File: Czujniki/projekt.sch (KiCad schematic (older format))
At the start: 79 parts, among them P1 CONN_01X08, P2 CONN_01X06, P3 CONN_01X05, T1 Si2323DS, T2 FDV303N, T3 FDV303N, T4 Si2323DS, T5 Si2323DS, T6 Si2323DS, T7 Si2323DS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

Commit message: All things on PCB.
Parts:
- removed DET2: MQ-Sensor, symbol MQ-Sensor
- removed R11: R, symbol R
- removed R12: 100K, symbol R_Small
- removed T6, T7: Si2323DS, symbol Si2323DS
- C10, C9: footprint (none) -> Capacitors_SMD:C_0805_HandSoldering
- DET1: footprint (none) -> Footprinty:MQ-sensor
- R10, R9: footprint (none) -> Resistors_SMD:R_0603
- T4, T5: footprint (none) -> Footprinty:SOT23
- U5: footprint (none) -> Footprinty:SOT23-mcp1700
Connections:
- no-connect marks 6 -> 8
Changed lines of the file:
@@
 $EndComp
-$Comp
-L MQ-Sensor DET2
-U 1 1 55B21DD7
-P 4900 8650
-F 0 "DET2" H 5050 8800 60  0000 C CNN
-F 1 "MQ-Sensor" V 4750 8350 60  0000 C CNN
-F 2 "" H 4900 8650 60  0000 C CNN
-F 3 "" H 4900 8650 60  0000 C CNN
-	1    4900 8650
-	1    0    0    -1
-$EndComp
-$Comp
-L R R11
-U 1 1 55B22225
-P 5150 8850
-F 0 "R11" V 5230 8850 50  0000 C CNN
-F 1 "R" V 5150 8850 50  0000 C CNN
-F 2 "" V 5080 8850 30  0000 C CNN
-F 3 "" H 5150 8850 30  0000 C CNN
-	1    5150 8850
-	1    0    0    -1
-$EndComp
-Wire Wire Line
-	5100 8650 5200 8650
-Wire Wire Line
-	5150 8650 5150 8700
 $Comp
 L MCP1702 U5
@@
 F 0 "U5" H 1950 5950 60  0000 C CNN
 F 1 "MCP1702" H 1850 6200 60  0000 C CNN
-F 2 "" H 1850 6050 60  0000 C CNN
+F 2 "Footprinty:SOT23-mcp1700" H 1850 6050 60  0001 C CNN
 F 3 "" H 1850 6050 60  0000 C CNN
 	1    1850 6100
 	1    0    0    -1
 $EndComp
-$Comp
-L Si2323DS T7
-U 1 1 55B2543A
-P 4900 8200
-F 0 "T7" H 4750 8350 39  0000 C CNN
-F 1 "Si2323DS" V 4950 8200 39  0000 C CNN
-F 2 "" H 4900 8200 39  0000 C CNN
-F 3 "" H 4900 8200 39  0000 C CNN
-	1    4900 8200
-	-1   0    0    1
-$EndComp
-Wire Wire Line
-	4900 7900 4900 8000
-$Comp
-L R_Small R12
-U 1 1 55B260F1
-P 5300 8200
-F 0 "R12" H 5330 8220 50  0000 L CNN
-F 1 "100K" H 5330 8160 50  0000 L CNN
-F 2 "" H 5300 8200 60  0000 C CNN
-F 3 "" H 5300 8200 60  0000 C CNN
-	1    5300 8200
-	0    -1   -1   0
-$EndComp
-Wire Wire Line
-	5100 8200 5200 8200
-Text GLabel 5450 8200 2    39   Input ~ 0
-DRV2
-Wire Wire Line
-	5450 8200 5400 8200
 $Comp
 L VDD #PWR076
@@
 $EndComp
 $Comp
-L GND #PWR078
-U 1 1 55B282A9
-P 5150 9050
-F 0 "#PWR078" H 5150 8800 50  0001 C CNN
-F 1 "GND" H 5150 8900 50  0000 C CNN
-F 2 "" H 5150 9050 60  0000 C CNN
-F 3 "" H 5150 9050 60  0000 C CNN
-	1    5150 9050
-	1    0    0    -1
-$EndComp
-Wire Wire Line
-	5150 9000 5150 9050
-$Comp
-L GND #PWR079
-U 1 1 55B28E36
-P 4900 9050
-F 0 "#PWR079" H 4900 8800 50  0001 C CNN
-F 1 "GND" H 4900 8900 50  0000 C CNN
-F 2 "" H 4900 9050 60  0000 C CNN
-F 3 "" H 4900 9050 60  0000 C CNN
-	1    4900 9050
-	1    0    0    -1
-$EndComp
-Wire Wire Line
-	4900 9050 4900 8850
-$Comp
-L Si2323DS T6
-U 1 1 55B29516
-P 4500 8200
-F 0 "T6" H 4350 8350 39  0000 C CNN
-F 1 "Si2323DS" V 4550 8200 39  0000 C CNN
-F 2 "" H 4500 8200 39  0000 C CNN
-F 3 "" H 4500 8200 39  0000 C CNN
-	1    4500 8200
-	-1   0    0    1
-$EndComp
-Wire Wire Line
-	4900 8400 4900 8450
-Wire Wire Line
-	5150 7950 5150 8200
-Wire Wire Line
-	5150 7950 4750 7950
-Wire Wire Line
-	4750 7950 4750 8200
-Wire Wire Line
-	4750 8200 4700 8200
-Connection ~ 5150 8200
-$Comp
 L VPP #PWR080
 U 1 1 55B2B4BE
@@
 $EndComp
 Wire Wire Line
-	4500 8000 4500 7900
-$Comp
-L VPP #PWR081
-U 1 1 55B2CA0B
-P 4900 7900
-F 0 "#PWR081" H 4900 7750 50  0001 C CNN
-F 1 "VPP" H 4900 8050 50  0000 C CNN
-F 2 "" H 4900 7900 60  0000 C CNN
-F 3 "" H 4900 7900 60  0000 C CNN
-	1    4900 7900
-	1    0    0    -1
-$EndComp
-Wire Wire Line
-	4500 8400 4500 8650
-Wire Wire Line
-	4500 8650 4700 8650
-$Comp
-L +5V #PWR082
-U 1 1 55B2D445
-P 4500 7900
-F 0 "#PWR082" H 4500 7750 50  0001 C CNN
-F 1 "+5V" H 4500 8040 50  0000 C CNN
-F 2 "" H 4500 7900 60  0000 C CNN
-F 3 "" H 4500 7900 60  0000 C CNN
-	1    4500 7900
-	1    0    0    -1
-$EndComp
-Wire Wire Line
 	2250 6050 2250 6150
 Wire Wire Line
@@
 F 0 "C10" H 2260 6320 50  0000 L CNN
 F 1 "1U" H 2260 6170 50  0000 L CNN
-F 2 "" H 2250 6250 60  0000 C CNN
+F 2 "Capacitors_SMD:C_0805_HandSoldering" H 2250 6250 60  0001 C CNN
 F 3 "" H 2250 6250 60  0000 C CNN
 	1    2250 6250
@@
 F 0 "C9" H 1460 6320 50  0000 L CNN
 F 1 "1U" H 1460 6170 50  0000 L CNN
-F 2 "" H 1450 6250 60  0000 C CNN
+F 2 "Capacitors_SMD:C_0805_HandSoldering" H 1450 6250 60  0001 C CNN
 F 3 "" H 1450 6250 60  0000 C CNN
 	1    1450 6250
@@
 F 0 "DET1" H 3250 8800 60  0000 C CNN
 F 1 "MQ-Sensor" V 2950 8350 60  0000 C CNN
-F 2 "" H 3100 8650 60  0000 C CNN
+F 2 "Footprinty:MQ-sensor" H 3100 8650 60  0001 C CNN
 F 3 "" H 3100 8650 60  0000 C CNN
 	1    3100 8650
@@
 F 0 "R9" V 3430 8850 50  0000 C CNN
 F 1 "4,7K" V 3350 8850 50  0000 C CNN
-F 2 "" V 3280 8850 30  0000 C CNN
+F 2 "Resistors_SMD:R_0603" V 3280 8850 30  0001 C CNN
 F 3 "" H 3350 8850 30  0000 C CNN
 	1    3350 8850
@@
 F 0 "T5" H 2950 8350 39  0000 C CNN
 F 1 "Si2323DS" V 3150 8200 39  0000 C CNN
-F 2 "" H 3100 8200 39  0000 C CNN
+F 2 "Footprinty:SOT23" H 3100 8200 39  0001 C CNN
 F 3 "" H 3100 8200 39  0000 C CNN
 	1    3100 8200
@@
 F 0 "R10" H 3530 8220 50  0000 L CNN
 F 1 "100K" H 3530 8160 50  0000 L CNN
-F 2 "" H 3500 8200 60  0000 C CNN
+F 2 "Resistors_SMD:R_0603" H 3500 8200 60  0001 C CNN
 F 3 "" H 3500 8200 60  0000 C CNN
 	1    3500 8200
@@
 F 0 "T4" H 2550 8350 39  0000 C CNN
 F 1 "Si2323DS" V 2750 8200 39  0000 C CNN
-F 2 "" H 2700 8200 39  0000 C CNN
+F 2 "Footprinty:SOT23" H 2700 8200 39  0001 C CNN
 F 3 "" H 2700 8200 39  0000 C CNN
 	1    2700 8200
@@
 SENSAN1
 Connection ~ 3350 8650
-Text GLabel 5200 8650 2    39   Input ~ 0
-SENSAN2
-Connection ~ 5150 8650
 Text GLabel 4150 2150 0    39   Input ~ 0
 SENSAN1
@@
 	4150 1450 4200 1450
 $Comp
-L PWR_FLAG #FLG?
+L PWR_FLAG #FLG089
 U 1 1 55B37391
 P 2450 6050
-F 0 "#FLG?" H 2450 6145 50  0001 C CNN
+F 0 "#FLG089" H 2450 6145 50  0001 C CNN
 F 1 "PWR_FLAG" H 2450 6230 50  0000 C CNN
 F 2 "" H 2450 6050 60  0000 C CNN
@@
 Wire Wire Line
 	2450 6100 2450 6050
+NoConn ~ 4200 1450
+NoConn ~ 4200 2050
 $EndSCHEMATC

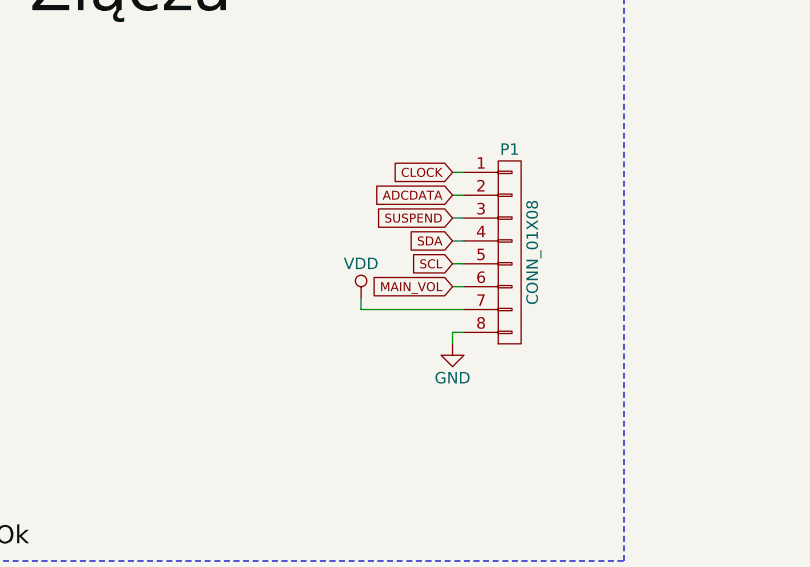
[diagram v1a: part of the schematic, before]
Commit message: GND on sensor board for routing.
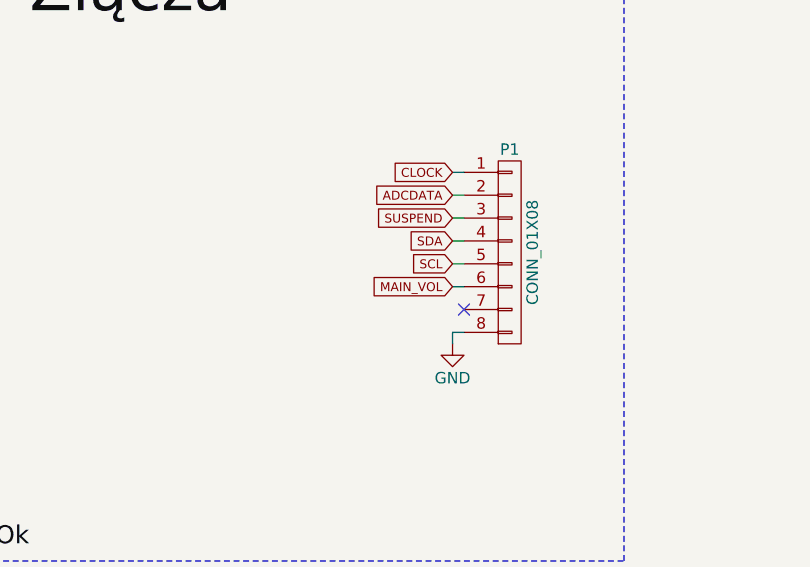
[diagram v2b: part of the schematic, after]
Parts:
- DET1: footprint Footprinty:MQ-sensor -> Socket_Strips:Socket_Strip_Straight_1x06
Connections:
- net VDD: no longer P1.7 (P7)
- no-connect marks 8 -> 9
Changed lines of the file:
@@
 F 0 "#PWR040" H 10150 7800 50  0001 C CNN
 F 1 "VDD" H 10150 8100 50  0000 C CNN
-F 2 "" H 10150 7950 60  0000 C CNN
+F 2 "~" H 10150 7950 60  0000 C CNN
 F 3 "" H 10150 7950 60  0000 C CNN
 	1    10150 7950
@@
 F 0 "#PWR041" H 9800 7800 50  0001 C CNN
 F 1 "VDD" H 9800 8100 50  0000 C CNN
-F 2 "" H 9800 7950 60  0000 C CNN
+F 2 "~" H 9800 7950 60  0000 C CNN
 F 3 "" H 9800 7950 60  0000 C CNN
 	1    9800 7950
@@
 	8750 9950 8750 10150
 Wire Wire Line
-	11200 2250 11200 2300
-Wire Wire Line
 	11600 2200 11650 2200
 Wire Wire Line
@@
 $Comp
 L VDD #PWR069
-U 1 1 55B1D959
-P 11200 2250
-F 0 "#PWR069" H 11200 2100 50  0001 C CNN
-F 1 "VDD" H 11200 2400 50  0000 C CNN
-F 2 "" H 11200 2250 60  0000 C CNN
-F 3 "" H 11200 2250 60  0000 C CNN
-	1    11200 2250
-	1    0    0    -1
-$EndComp
-$Comp
-L VDD #PWR070
 U 1 1 55B1DBFD
 P 11600 4150
-F 0 "#PWR070" H 11600 4000 50  0001 C CNN
+F 0 "#PWR069" H 11600 4000 50  0001 C CNN
 F 1 "VDD" H 11600 4300 50  0000 C CNN
 F 2 "" H 11600 4150 60  0000 C CNN
@@
 $EndComp
 $Comp
-L VDD #PWR071
+L VDD #PWR070
 U 1 1 55B1E367
 P 12250 6550
-F 0 "#PWR071" H 12250 6400 50  0001 C CNN
+F 0 "#PWR070" H 12250 6400 50  0001 C CNN
 F 1 "VDD" H 12250 6700 50  0000 C CNN
 F 2 "" H 12250 6550 60  0000 C CNN
@@
 $EndComp
 $Comp
-L VDD #PWR072
+L VDD #PWR071
 U 1 1 55B1E4BC
 P 9800 4450
-F 0 "#PWR072" H 9800 4300 50  0001 C CNN
+F 0 "#PWR071" H 9800 4300 50  0001 C CNN
 F 1 "VDD" H 9800 4600 50  0000 C CNN
 F 2 "" H 9800 4450 60  0000 C CNN
@@
 $EndComp
 $Comp
-L VDD #PWR073
+L VDD #PWR072
 U 1 1 55B1EEA8
 P 5650 5400
-F 0 "#PWR073" H 5650 5250 50  0001 C CNN
+F 0 "#PWR072" H 5650 5250 50  0001 C CNN
 F 1 "VDD" H 5650 5550 50  0000 C CNN
 F 2 "" H 5650 5400 60  0000 C CNN
@@
 	4550 5700 4550 5900
 $Comp
-L GND #PWR074
+L GND #PWR073
 U 1 1 55B1FDEB
 P 4550 5900
-F 0 "#PWR074" H 4550 5650 50  0001 C CNN
+F 0 "#PWR073" H 4550 5650 50  0001 C CNN
 F 1 "GND" H 4550 5750 50  0000 C CNN
 F 2 "" H 4550 5900 60  0000 C CNN
@@
 $EndComp
 $Comp
-L GND #PWR075
+L GND #PWR074
 U 1 1 55B1FF3B
 P 5650 5900
-F 0 "#PWR075" H 5650 5650 50  0001 C CNN
+F 0 "#PWR074" H 5650 5650 50  0001 C CNN
 F 1 "GND" H 5650 5750 50  0000 C CNN
 F 2 "" H 5650 5900 60  0000 C CNN
@@
 	1    0    0    -1
 $EndComp
-Wire Wire Line
-	11200 2300 11650 2300
 $Comp
 L C_Small C8
@@
 $EndComp
 $Comp
-L VDD #PWR076
+L VDD #PWR075
 U 1 1 55B27420
 P 1450 6050
-F 0 "#PWR076" H 1450 5900 50  0001 C CNN
+F 0 "#PWR075" H 1450 5900 50  0001 C CNN
 F 1 "VDD" H 1450 6200 50  0000 C CNN
 F 2 "" H 1450 6050 60  0000 C CNN
@@
 	1450 6100 1500 6100
 $Comp
-L GND #PWR077
+L GND #PWR076
 U 1 1 55B27E7A
 P 1850 6450
-F 0 "#PWR077" H 1850 6200 50  0001 C CNN
+F 0 "#PWR076" H 1850 6200 50  0001 C CNN
 F 1 "GND" H 1850 6300 50  0000 C CNN
 F 2 "" H 1850 6450 60  0000 C CNN
@@
 $EndComp
 $Comp
-L VPP #PWR080
+L VPP #PWR077
 U 1 1 55B2B4BE
 P 2250 6050
-F 0 "#PWR080" H 2250 5900 50  0001 C CNN
+F 0 "#PWR077" H 2250 5900 50  0001 C CNN
 F 1 "VPP" H 2250 6200 50  0000 C CNN
 F 2 "" H 2250 6050 60  0000 C CNN
@@
 Connection ~ 2250 6100
 $Comp
-L GND #PWR083
+L GND #PWR078
 U 1 1 55B2FC1D
 P 1450 6450
-F 0 "#PWR083" H 1450 6200 50  0001 C CNN
+F 0 "#PWR078" H 1450 6200 50  0001 C CNN
 F 1 "GND" H 1450 6300 50  0000 C CNN
 F 2 "" H 1450 6450 60  0000 C CNN
@@
 	1450 6450 1450 6350
 $Comp
-L GND #PWR084
+L GND #PWR079
 U 1 1 55B2FE91
 P 2250 6450
-F 0 "#PWR084" H 2250 6200 50  0001 C CNN
+F 0 "#PWR079" H 2250 6200 50  0001 C CNN
 F 1 "GND" H 2250 6300 50  0000 C CNN
 F 2 "" H 2250 6450 60  0000 C CNN
@@
 F 0 "DET1" H 3250 8800 60  0000 C CNN
 F 1 "MQ-Sensor" V 2950 8350 60  0000 C CNN
-F 2 "Footprinty:MQ-sensor" H 3100 8650 60  0001 C CNN
+F 2 "Socket_Strips:Socket_Strip_Straight_1x06" H 3100 8650 60  0001 C CNN
 F 3 "" H 3100 8650 60  0000 C CNN
 	1    3100 8650
@@
 	3650 8200 3600 8200
 $Comp
-L GND #PWR085
+L GND #PWR080
 U 1 1 55B31A46
 P 3350 9050
-F 0 "#PWR085" H 3350 8800 50  0001 C CNN
+F 0 "#PWR080" H 3350 8800 50  0001 C CNN
 F 1 "GND" H 3350 8900 50  0000 C CNN
 F 2 "" H 3350 9050 60  0000 C CNN
@@
 	3350 9000 3350 9050
 $Comp
-L GND #PWR086
+L GND #PWR081
 U 1 1 55B31A4D
 P 3100 9050
-F 0 "#PWR086" H 3100 8800 50  0001 C CNN
+F 0 "#PWR081" H 3100 8800 50  0001 C CNN
 F 1 "GND" H 3100 8900 50  0000 C CNN
 F 2 "" H 3100 9050 60  0000 C CNN
@@
 	2700 8000 2700 7900
 $Comp
-L VPP #PWR087
+L VPP #PWR082
 U 1 1 55B31A61
 P 3100 7900
-F 0 "#PWR087" H 3100 7750 50  0001 C CNN
+F 0 "#PWR082" H 3100 7750 50  0001 C CNN
 F 1 "VPP" H 3100 8050 50  0000 C CNN
 F 2 "" H 3100 7900 60  0000 C CNN
@@
 	2700 8650 2900 8650
 $Comp
-L +5V #PWR088
+L +5V #PWR083
 U 1 1 55B31A69
 P 2700 7900
-F 0 "#PWR088" H 2700 7750 50  0001 C CNN
+F 0 "#PWR083" H 2700 7750 50  0001 C CNN
 F 1 "+5V" H 2700 8040 50  0000 C CNN
 F 2 "" H 2700 7900 60  0000 C CNN
@@
 	4150 1450 4200 1450
 $Comp
-L PWR_FLAG #FLG089
+L PWR_FLAG #FLG084
 U 1 1 55B37391
 P 2450 6050
-F 0 "#FLG089" H 2450 6145 50  0001 C CNN
+F 0 "#FLG084" H 2450 6145 50  0001 C CNN
 F 1 "PWR_FLAG" H 2450 6230 50  0000 C CNN
 F 2 "" H 2450 6050 60  0000 C CNN
@@
 NoConn ~ 4200 1450
 NoConn ~ 4200 2050
+NoConn ~ 11650 2300
 $EndSCHEMATC

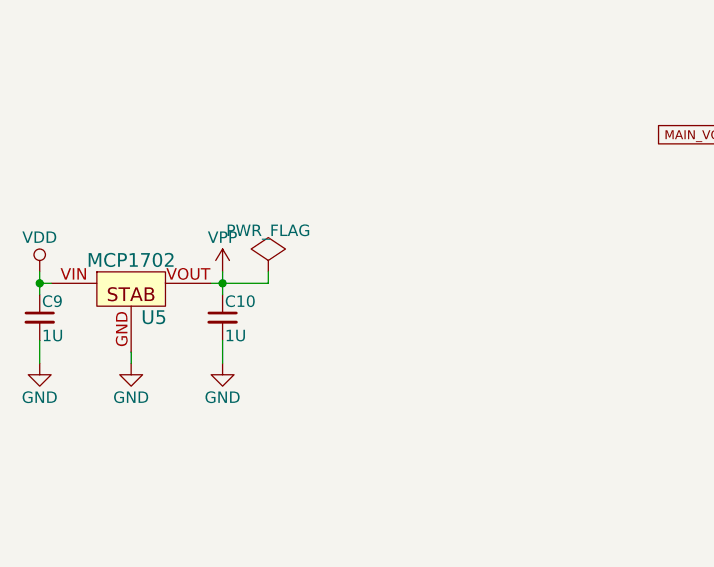
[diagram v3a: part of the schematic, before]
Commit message: Change board sizes.
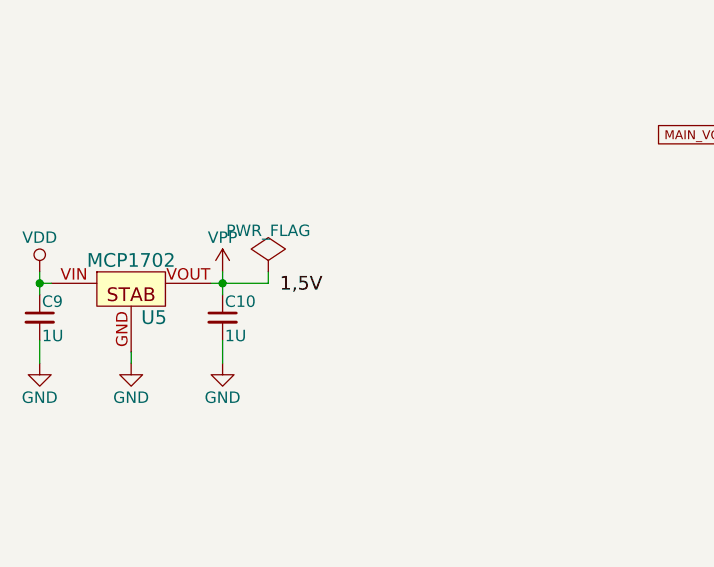
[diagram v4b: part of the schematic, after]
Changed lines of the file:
@@
 NoConn ~ 4200 2050
 NoConn ~ 11650 2300
+Text Label 2500 6150 0    60   ~ 0
+1,5V
 $EndSCHEMATC

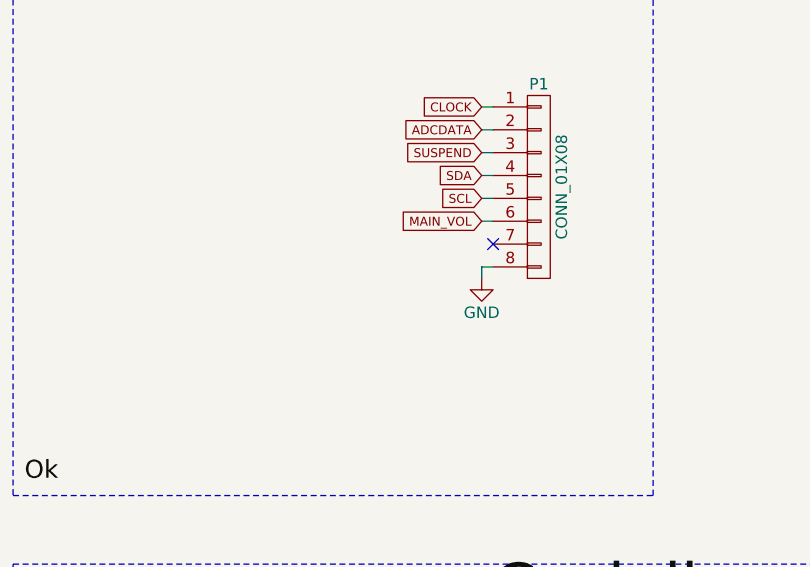
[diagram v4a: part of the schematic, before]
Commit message: Changed switch placement (from main to sensor board)
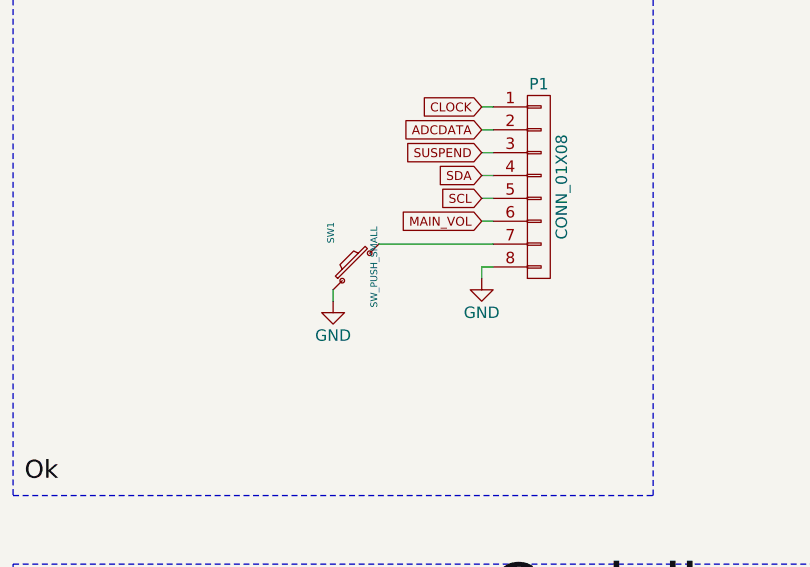
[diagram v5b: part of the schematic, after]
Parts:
- added SW1: SW_PUSH_SMALL, Footprinty:TACT_SW_ONE_PAIR, symbol SW_PUSH_SMALL
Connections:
- net GND: now also SW1.1
- net at P1.7 (P7): now also SW1.2
- no-connect marks 9 -> 8
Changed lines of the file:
@@
 NoConn ~ 4200 1450
 NoConn ~ 4200 2050
-NoConn ~ 11650 2300
 Text Label 2500 6150 0    60   ~ 0
 1,5V
+$Comp
+L SW_PUSH_SMALL SW1
+U 1 1 55B90838
+P 11050 2400
+F 0 "SW1" H 11200 2510 30  0000 C CNN
+F 1 "SW_PUSH_SMALL" H 11050 2321 30  0000 C CNN
+F 2 "Footprinty:TACT_SW_ONE_PAIR" H 11050 2400 60  0001 C CNN
+F 3 "" H 11050 2400 60  0000 C CNN
+	1    11050 2400
+	0    -1   -1   0
+$EndComp
+$Comp
+L GND #PWR085
+U 1 1 55B929EB
+P 10950 2550
+F 0 "#PWR085" H 10950 2300 50  0001 C CNN
+F 1 "GND" H 10950 2400 50  0000 C CNN
+F 2 "" H 10950 2550 60  0000 C CNN
+F 3 "" H 10950 2550 60  0000 C CNN
+	1    10950 2550
+	1    0    0    -1
+$EndComp
+Wire Wire Line
+	10950 2550 10950 2500
+Wire Wire Line
+	11650 2300 11150 2300
 $EndSCHEMATC
